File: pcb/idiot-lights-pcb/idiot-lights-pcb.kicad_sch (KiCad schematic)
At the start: 39 parts, among them SW1 Toggle left indicator, SW2 Toggle right indicator, SW3 Toggle hazard warning, SW4 Break control, SW5 Reset

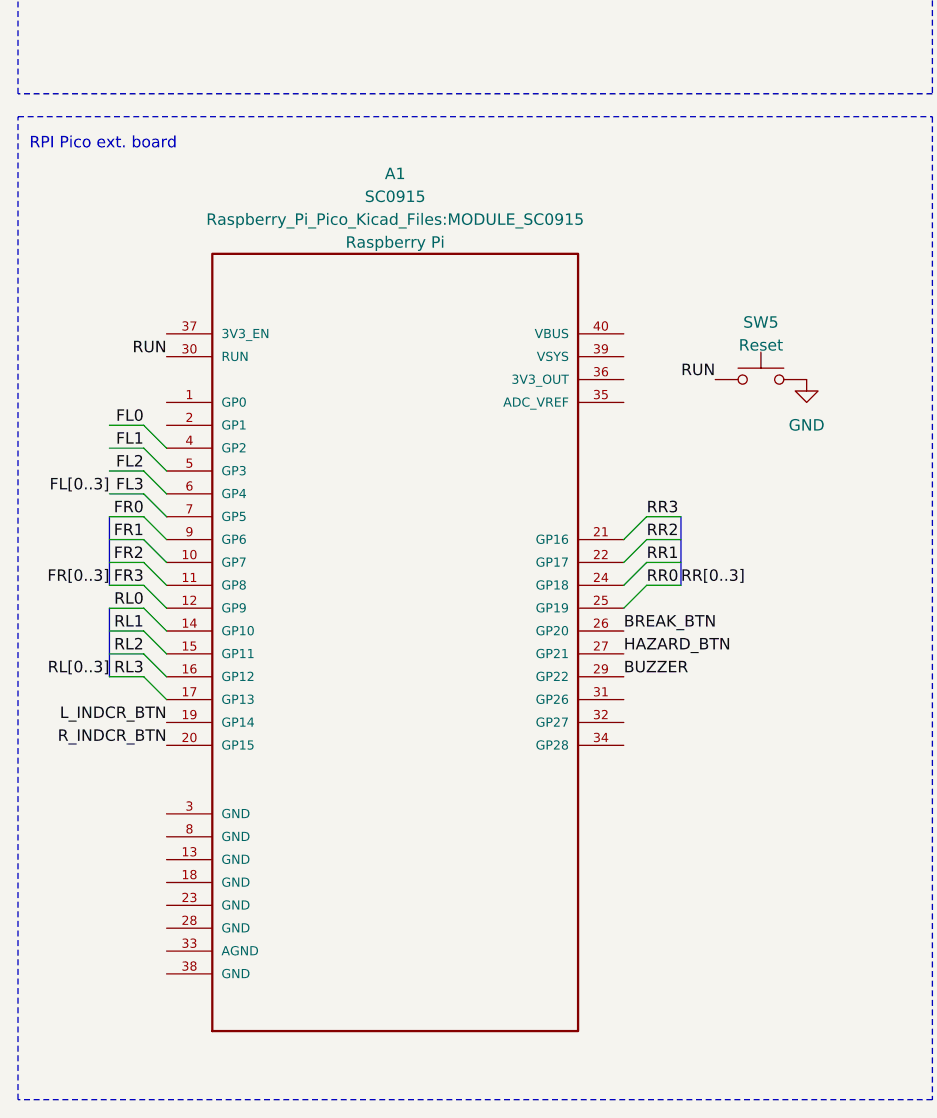
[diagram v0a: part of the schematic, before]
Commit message: Add pico SMD solder mounts
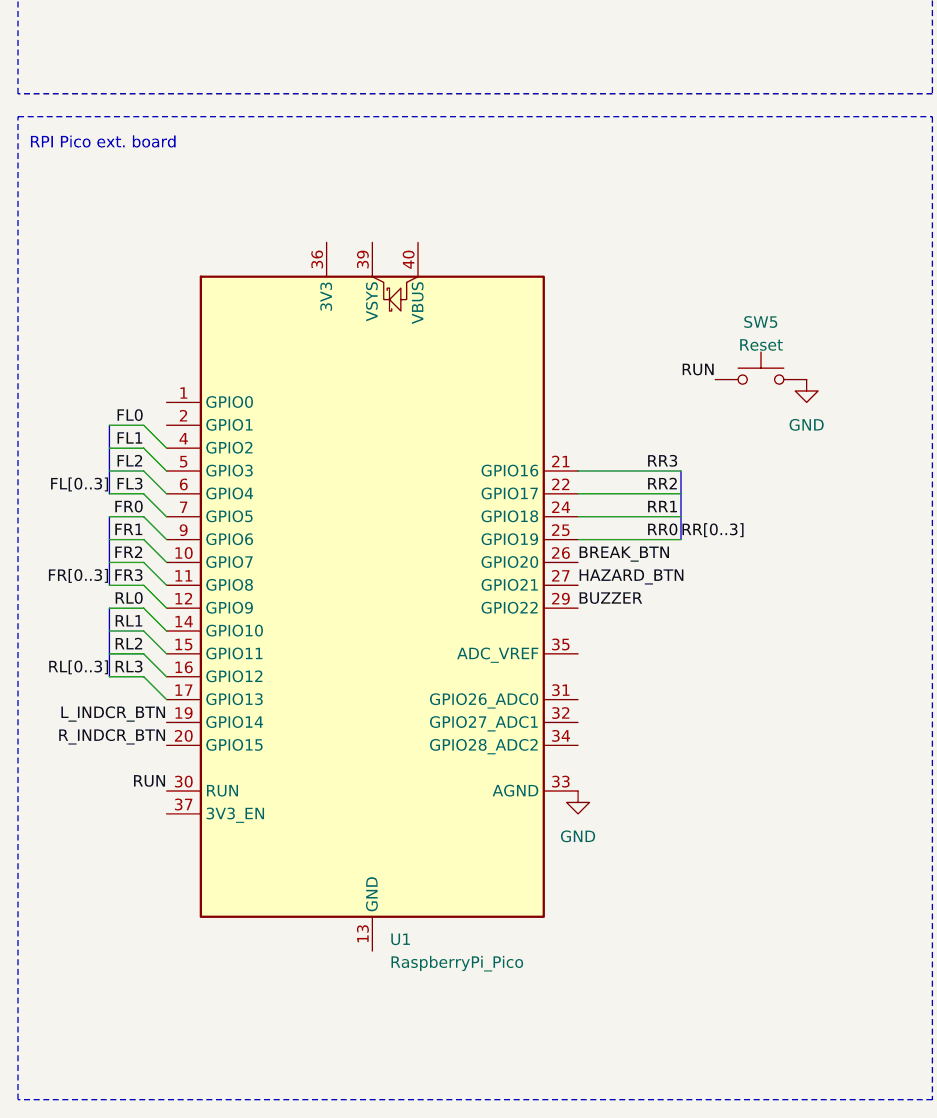
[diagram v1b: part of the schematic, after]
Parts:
- removed A1: SC0915, Raspberry_Pi_Pico_Kicad_Files:MODULE_SC0915, symbol Raspberry_Pi_Pico_SC0915:SC0915
- added U1: RaspberryPi_Pico, Module_RaspberryPi_Pico:RaspberryPi_Pico_Common, symbol MCU_Module_RaspberryPi_Pico:RaspberryPi_Pico
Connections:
- net BREAK_BTN: now also U1.26 (GPIO20)
- net BUZZER: now also U1.29 (GPIO22)
- net GND: now also U1.33 (AGND)
- net HAZARD_BTN: now also U1.27 (GPIO21)
- net L_INDCR_BTN: now also U1.19 (GPIO14)
- net RR0: now also U1.21 (GPIO16), U1.25 (GPIO19)
- net RR1: now also U1.24 (GPIO18)
- net RR2: now also U1.22 (GPIO17)
- net RUN: now also U1.30 (RUN)
- net R_INDCR_BTN: now also U1.20 (GPIO15)
- new net: U1.13 (GND), U1.18 (GND), U1.23 (GND), U1.28 (GND), U1.3 (GND), U1.38 (GND), U1.8 (GND)

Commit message: Replace buzzer with CPT
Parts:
- BZ1: footprint Buzzer_Beeper:PUIAudio_SMT_0825_S_4_R -> Buzzer_Beeper:Buzzer_CUI_CPT-9019S-SMT
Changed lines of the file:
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@@
       (effects (font (size 1.27 1.27)) (justify left))
     )
-    (property "Footprint" "Buzzer_Beeper:PUIAudio_SMT_0825_S_4_R" (at 169.545 97.79 90)
+    (property "Footprint" "Buzzer_Beeper:Buzzer_CUI_CPT-9019S-SMT" (at 169.545 97.79 90)
       (effects (font (size 1.27 1.27)) hide)
     )

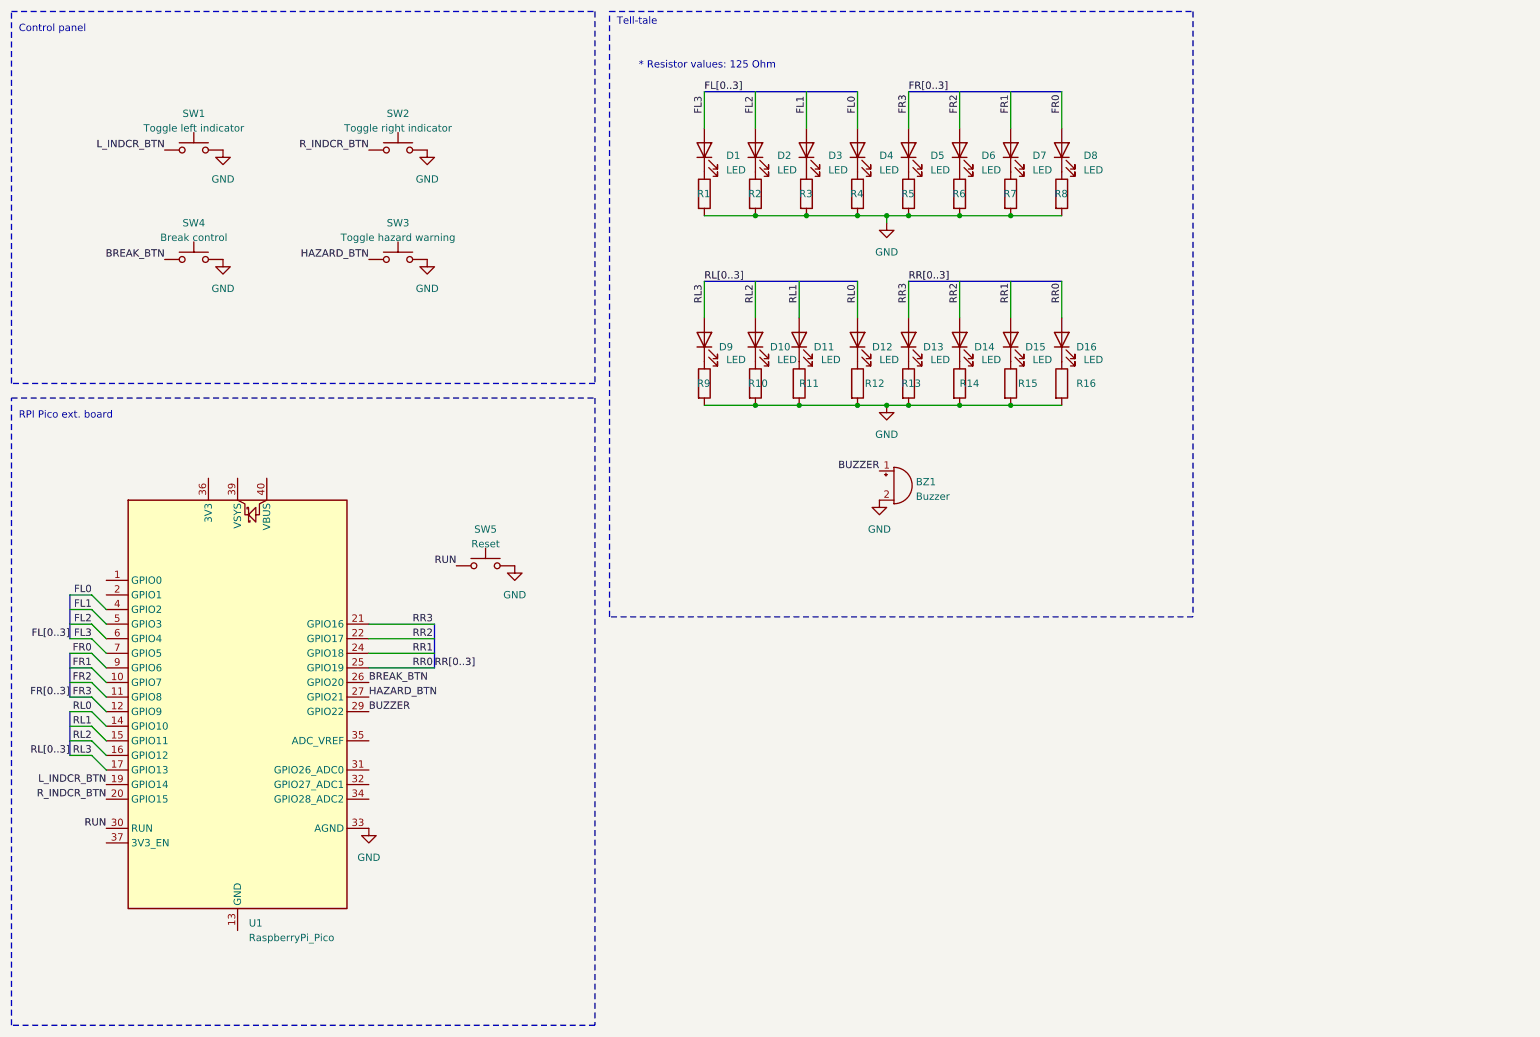
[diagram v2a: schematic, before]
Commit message: Add mosfet controlling every LED and let 5V rail handle powering
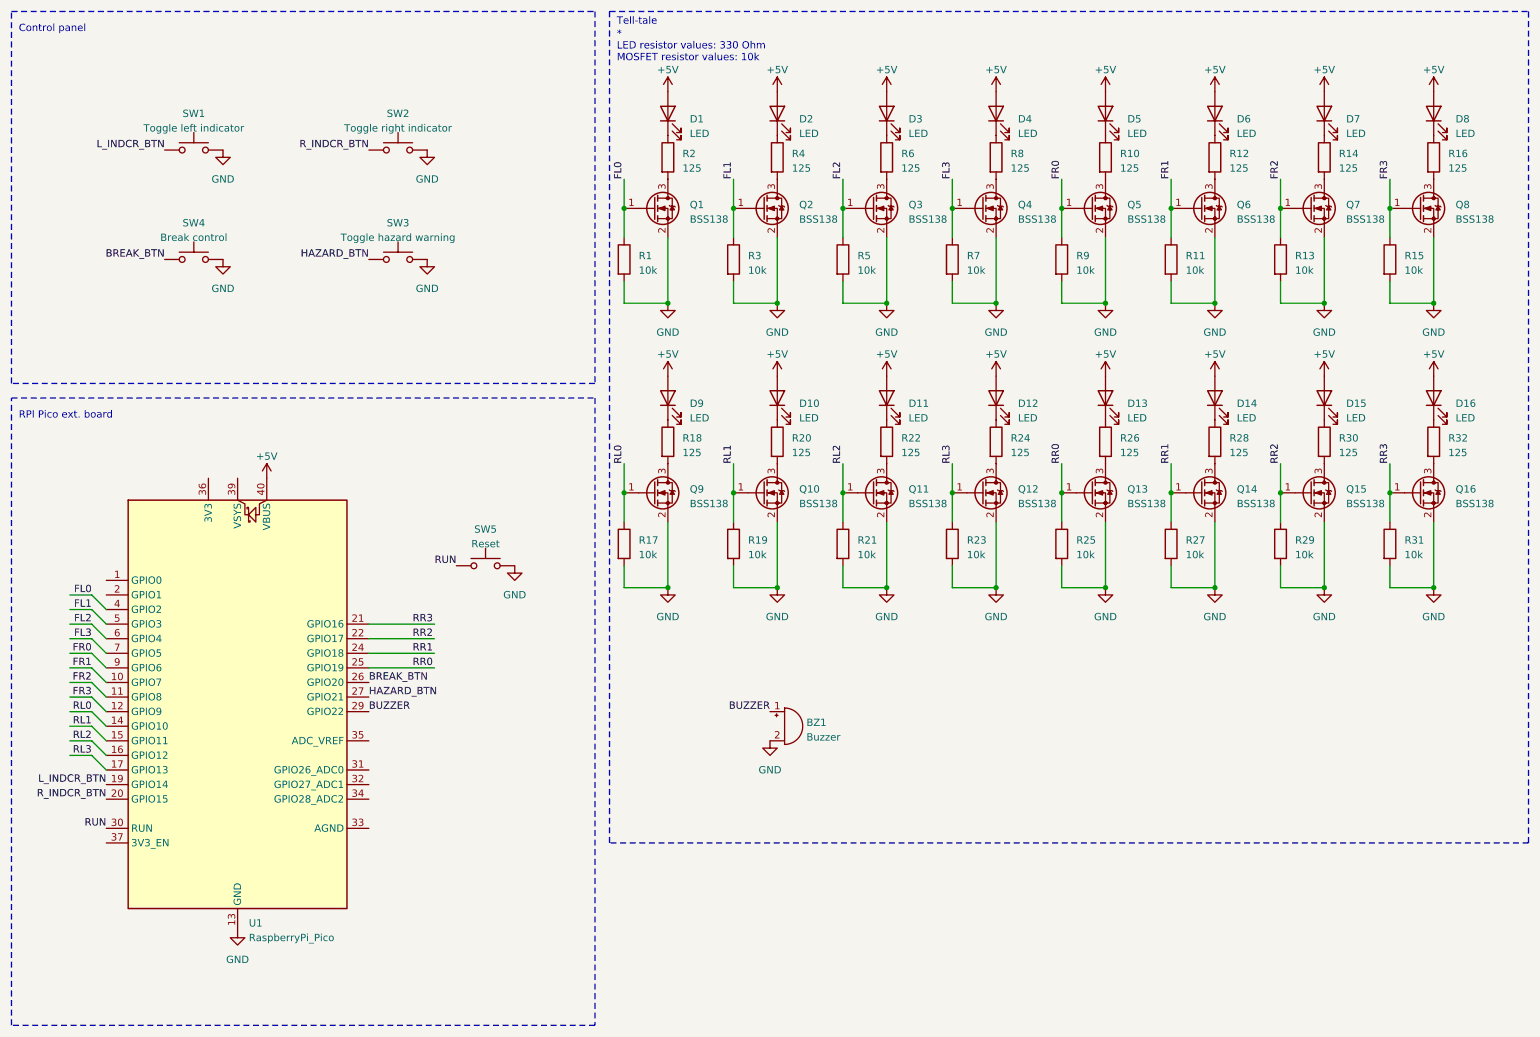
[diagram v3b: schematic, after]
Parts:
- added Q1, Q10, Q11, Q12, Q13, Q14, Q15, Q16, Q2, Q3, Q4, Q5, Q6, Q7, Q8, Q9: BSS138, Package_TO_SOT_SMD_no_silk:SOT-23_no_silk, symbol Transistor_FET:BSS138
- added R17, R19, R21, R23, R25, R27, R29, R31: 10k, Resistor_SMD_no_silk:R_0603_1608Metric_no_silk, symbol Device:R
- added R18, R20, R22, R24, R26, R28, R30, R32: 125, Resistor_SMD_no_silk:R_0603_1608Metric_no_silk, symbol Device:R
- R1, R11, R13, R15, R3, R5, R7, R9: value 125 -> 10k; footprint Resistor_SMD:R_0805_2012Metric_Pad1.20x1.40mm_HandSolder -> Resistor_SMD_no_silk:R_0603_1608Metric_no_silk
- R10, R12, R14, R16, R2, R4, R6, R8: footprint Resistor_SMD:R_0805_2012Metric_Pad1.20x1.40mm_HandSolder -> Resistor_SMD_no_silk:R_0603_1608Metric_no_silk
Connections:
- net FL0: now also R1.1, Q1.1 (G); no longer D4.2 (A)
- net FL1: now also R3.1, Q2.1 (G); no longer D3.2 (A)
- net FL2: now also R5.1, Q3.1 (G); no longer D2.2 (A)
- net FL3: now also R7.1, Q4.1 (G); no longer D1.2 (A)
- net FR0: now also R9.1, Q5.1 (G); no longer D8.2 (A)
- net FR1: now also R11.1, Q6.1 (G); no longer D7.2 (A)
- net FR2: now also R13.1, Q7.1 (G); no longer D6.2 (A)
- net FR3: now also R15.1, Q8.1 (G); no longer D5.2 (A)
- net GND: now also U1.13 (GND), U1.18 (GND), U1.23 (GND), U1.28 (GND), U1.3 (GND), U1.38 (GND), U1.8 (GND), Q1.2 (S), Q10.2 (S), Q11.2 (S), Q12.2 (S), Q13.2 (S), Q14.2 (S), Q15.2 (S), Q16.2 (S), Q2.2 (S), Q3.2 (S), Q4.2 (S), Q5.2 (S), Q6.2 (S), Q7.2 (S), Q8.2 (S), Q9.2 (S), R17.2, R19.2, R21.2, R23.2, R25.2, R27.2, R29.2, R31.2; no longer R10.2, R12.2, R14.2, R16.2, R2.2, R4.2, R6.2, R8.2, U1.33 (AGND)
- net RL0: now also Q9.1 (G), R17.1; no longer D12.2 (A)
- net RL1: now also Q10.1 (G), R19.1; no longer D11.2 (A)
- net RL2: now also Q11.1 (G), R21.1; no longer D10.2 (A)
- net RL3: now also Q12.1 (G), R23.1; no longer D9.2 (A)
- net RR0: now also Q13.1 (G), R25.1; no longer D13.2 (A), D16.2 (A), U1.21 (GPIO16)
- net RR1: now also Q14.1 (G), R27.1; no longer D15.2 (A)
- net RR2: now also Q15.1 (G), R29.1; no longer D14.2 (A)
- net at D3.1 (K): now also R6.1; no longer R3.1
- net at R8.1: now also D4.1 (K); no longer D8.1 (K)
- net at R4.1: now also D2.1 (K); no longer D4.1 (K)
- net at D15.1 (K): now also R30.1; no longer R15.1
- net at D12.1 (K): now also R24.1; no longer R12.1
- net at D13.1 (K): now also R26.1; no longer R13.1
- net at D1.1 (K): now also R2.1; no longer R1.1
- net at D9.1 (K): now also R18.1; no longer R9.1
- net at D11.1 (K): now also R22.1; no longer R11.1
- net at D7.1 (K): now also R14.1; no longer R7.1
- net at D16.1 (K): now also R32.1; no longer R16.1
- net at R10.1: now also D5.1 (K); no longer D10.1 (K)
- net at D14.1 (K): now also R28.1; no longer R14.1
- net at D6.1 (K): now also R12.1; no longer R6.1
- net +5V: now reaches U1.40 (VBUS)
- net +5V: now also D1.2 (A), D10.2 (A), D11.2 (A), D12.2 (A), D13.2 (A), D14.2 (A), D15.2 (A), D16.2 (A), D2.2 (A), D3.2 (A), D4.2 (A), D5.2 (A), D6.2 (A), D7.2 (A), D8.2 (A), D9.2 (A)
- new net: Q13.3 (D), R26.2
- new net: Q15.3 (D), R30.2
- new net: Q2.3 (D), R4.2
- new net: Q1.3 (D), R2.2
- new net: Q10.3 (D), R20.2
- new net: Q7.3 (D), R14.2
- new net: Q5.3 (D), R10.2
- new net: Q9.3 (D), R18.2
- new net: Q11.3 (D), R22.2
- new net: Q16.3 (D), R32.2
- new net: Q3.3 (D), R6.2
- new net: Q12.3 (D), R24.2
- new net: Q14.3 (D), R28.2
- new net: D10.1 (K), R20.1
- new net: Q8.3 (D), R16.2
- new net: D8.1 (K), R16.1
- new net: Q4.3 (D), R8.2
- new net: Q6.3 (D), R12.2
- new net RR3: Q16.1 (G), R31.1, U1.21 (GPIO16)
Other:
- note added: "* LED resistor values: 330 Ohm MOSFET resistor values: 10k"
- note removed: "* Resistor values: 125 Ohm"
- moved on the sheet: BZ1

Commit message: Add MPN field and generate bom
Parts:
- BZ1: MPN (none) -> CPT-9019B-SMT-TR
- D1, D10, D11, D12, D13, D14, D15, D16, D2, D3, D4, D5, D6, D7, D8, D9: MPN (none) -> APTD1608SYCK/J3-PF
- Q1, Q10, Q11, Q12, Q13, Q14, Q15, Q16, Q2, Q3, Q4, Q5, Q6, Q7, Q8, Q9: MPN (none) -> BSS138
- R1, R11, R13, R15, R17, R19, R21, R23, R25, R27, R29, R3, R31, R5, R7, R9: MPN (none) -> (none)
- R10, R12, R14, R16, R18, R2, R20, R22, R24, R26, R28, R30, R32, R4, R6, R8: value 125 -> 150; MPN (none) -> (none)
- SW1, SW2, SW3, SW4, SW5: MPN (none) -> 1301.9315
- U1: MPN (none) -> RASPBERRY PI PICO
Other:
- note added: "* LED values: 150 Ohm (20mA forward current) MOSFET resistor values: 10k"
- note removed: "* LED resistor values: 330 Ohm MOSFET resistor values: 10k"
